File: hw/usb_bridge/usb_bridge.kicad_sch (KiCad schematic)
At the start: 61 parts, among them J1 USB_C_Receptacle_USB2.0_14P, J2 DE9, U1 CH340E, U2 MAX485E, U3 CH334R, U5 MCP1754S-3302xCB, U6 TJA1051T-3, U8 74HC04, Y1 HCI XC53G2-12.000-F20LJDT

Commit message: usb_bridge: Replace LCSC part codes for USB TVS diodes
Signed-off-by: Mateusz Pajak <22417805+Tai-Min@users.noreply.github.com>
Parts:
- D2, D3: LCSC Part # C110752 -> C21713982
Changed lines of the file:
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@@
 			)
 		)
-		(property "LCSC Part #" "C110752"
+		(property "LCSC Part #" "C21713982"
 			(at 72.39 73.66 90)
 			(effects
@@
 			)
 		)
-		(property "LCSC Part #" "C110752"
+		(property "LCSC Part #" "C21713982"
 			(at 66.04 67.31 90)
 			(effects

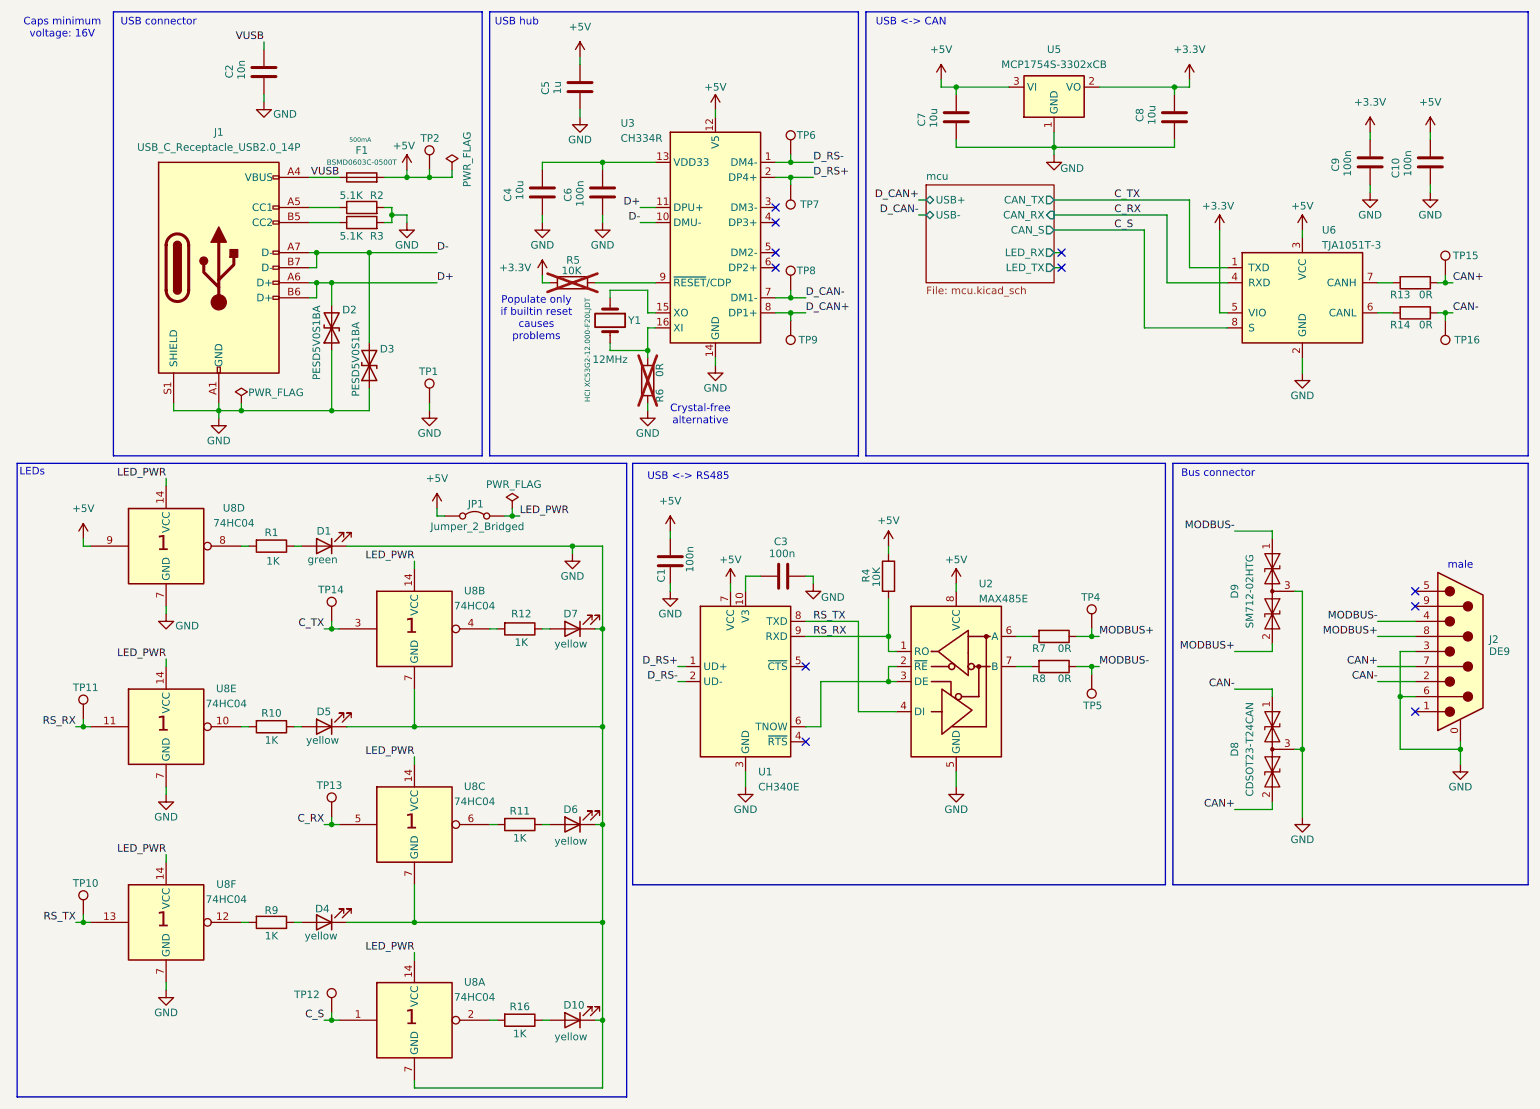
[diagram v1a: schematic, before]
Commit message: usb_bridge: Major LED fixes, replace USB-C protection circuit, add RS485 pullups, add mounting holes
Signed-off-by: Mateusz Pajak <22417805+Tai-Min@users.noreply.github.com>
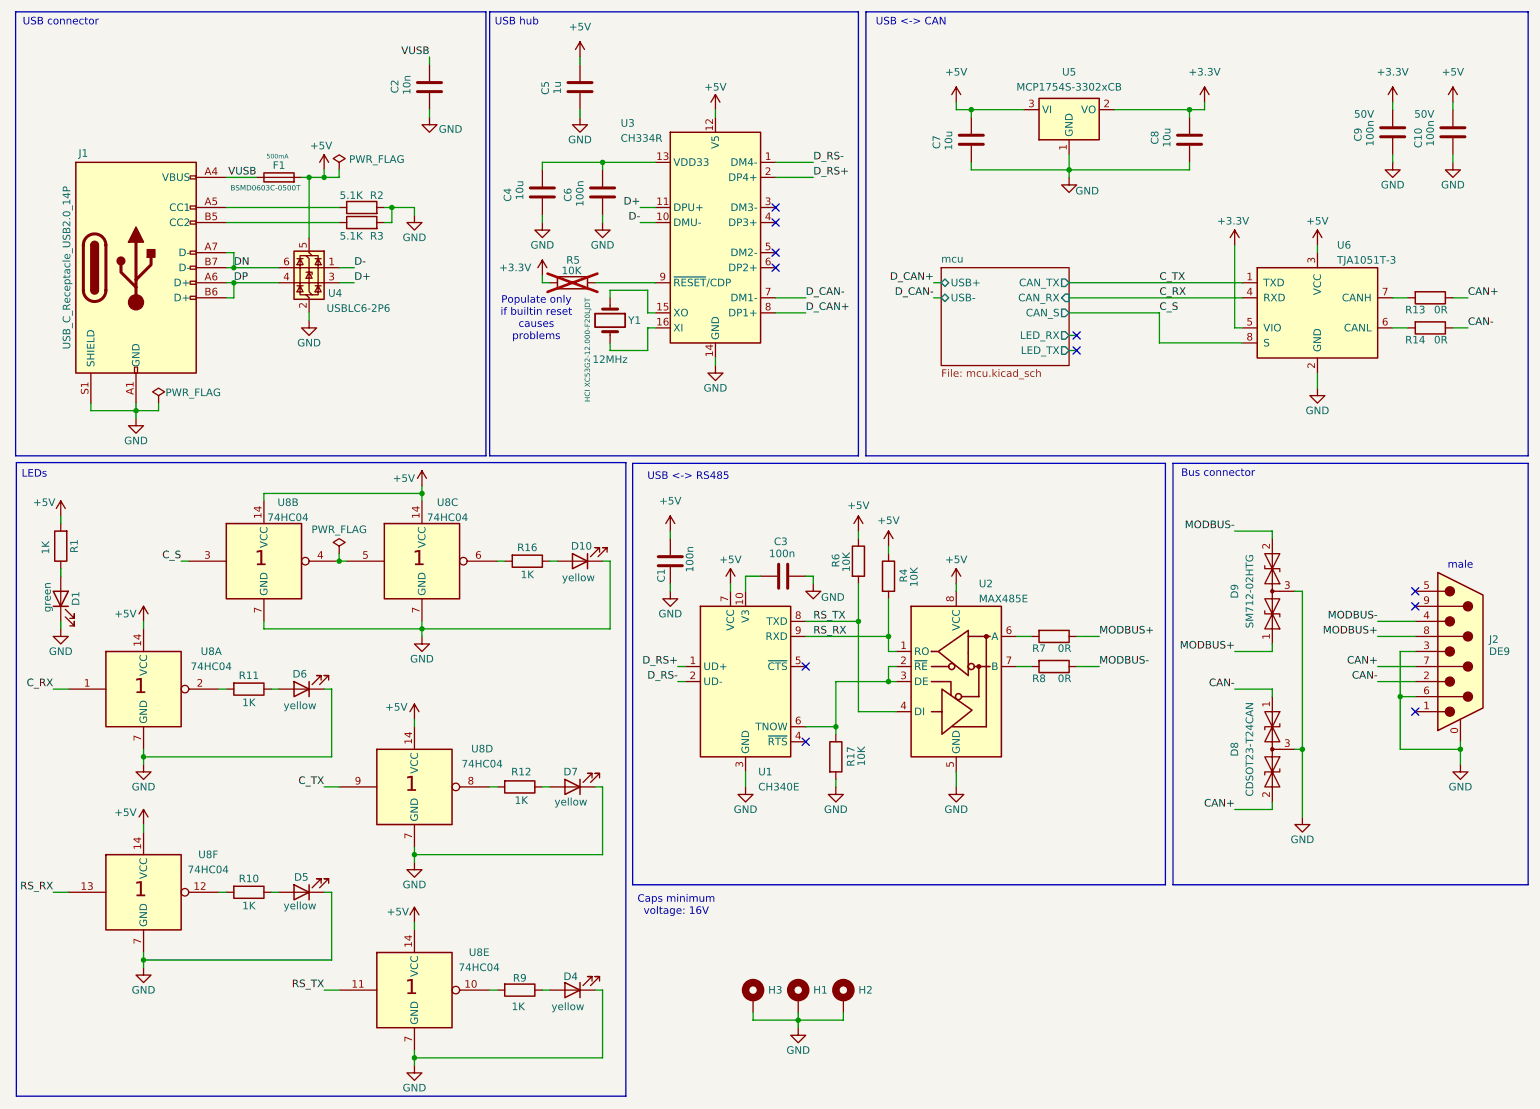
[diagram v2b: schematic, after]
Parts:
- removed D2, D3: PESD5V0S1BA, Diode_SMD:D_SOD-323_HandSoldering, symbol Device:D_TVS
- removed JP1: Jumper_2_Bridged, Jumper:SolderJumper-2_P1.3mm_Bridged_RoundedPad1.0x1.5mm, symbol Jumper:Jumper_2_Bridged
- removed TP1, TP10, TP11, TP12, TP13, TP14, TP15, TP16, TP2, TP4, TP5, TP6, TP7, TP8, TP9: TestPoint, TestPoint:TestPoint_Pad_D1.5mm, symbol Connector:TestPoint
- added H1, H2, H3: MountingHole_Pad, MountingHole:MountingHole_3.2mm_M3_Pad_Via, symbol Mechanical:MountingHole_Pad
- added R17: 10K, Resistor_SMD:R_0603_1608Metric, symbol Device:R
- added U4: USBLC6-2P6, Package_TO_SOT_SMD:SOT-666, symbol Power_Protection:USBLC6-2P6
- R6: value 0R -> 10K; LCSC Part # C95177 -> C98220; now fitted
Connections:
- net LED_PWR is gone; now on net +5V: U8.14 (VCC), U8.14 (VCC), U8.14 (VCC), U8.14 (VCC), U8.14 (VCC), U8.14 (VCC)
- net +5V: now also R1.2, R6.1, U4.5 (VBUS); no longer U8.9
- net C_RX: now also U8.1; no longer U8.5
- net C_S: now also U8.3; no longer U8.1
- net C_TX: now also U8.9; no longer U8.3
- net D+: now also U4.3 (I/O2); no longer J1.A6 (D+), J1.B6 (D+)
- net D-: now also U4.1 (I/O1); no longer J1.A7 (D-), J1.B7 (D-)
- net GND: now also H1.1, H2.1, H3.1, R17.2, U4.2 (GND); no longer R6.2
- net MODBUS+: now also D9.1 (A1); no longer D9.2 (A2)
- net MODBUS-: now also D9.2 (A2); no longer D9.1 (A1)
- net RS_RX: now also U8.13; no longer U8.11
- net RS_TX: now also R6.2, U8.11; no longer U8.13
- net at U8.8: now also R12.2; no longer R1.2
- net at U8.12: now also R10.2; no longer R9.2
- net at U8.4: now also U8.5; no longer R12.2
- net at U3.16 (XI), Y1.2: no longer R6.1
- net at U1.6 (TNOW), U2.2 (~{RE}), U2.3 (DE): now also R17.1
- net at U8.10: now also R9.2; no longer R10.2
- net at U8.2: now also R11.2; no longer R16.2
- net at U8.6: now also R16.2; no longer R11.2
- new net DN: J1.A7 (D-), J1.B7 (D-), U4.6 (I/O1)
- new net DP: J1.A6 (D+), J1.B6 (D+), U4.4 (I/O2)
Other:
- note removed: "Crystal-free alternative"
- moved on the sheet: C10, C2, C7, C8, C9, D1, D10, D4, D5, D6, D7, F1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

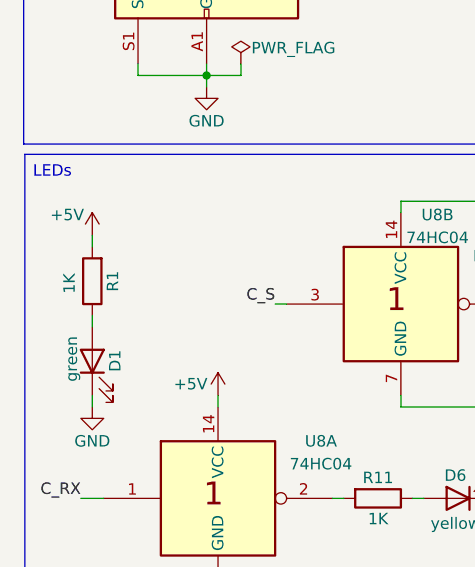
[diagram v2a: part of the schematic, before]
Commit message: Remove residual silkscreen from the bottom, replace LED resistor to 10K
Signed-off-by: Tai-Min <22417805+Tai-Min@users.noreply.github.com>
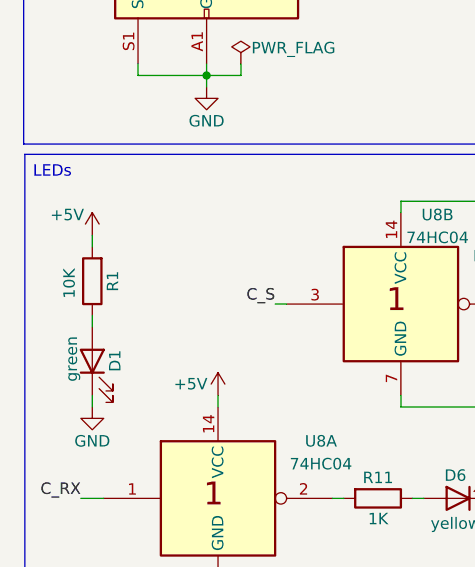
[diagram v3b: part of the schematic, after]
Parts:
- R1: value 1K -> 10K; LCSC Part # C22548 -> C98220
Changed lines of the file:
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@@
 			)
 		)
-		(property "Value" "1K"
+		(property "Value" "10K"
 			(at 17.78 104.394 90)
 			(effects
@@
 			)
 		)
-		(property "LCSC Part #" "C22548"
+		(property "LCSC Part #" "C98220"
 			(at 20.32 104.14 90)
 			(effects
